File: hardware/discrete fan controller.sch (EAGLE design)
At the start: 13 parts, among them Q1 BCX56, U1 TL431

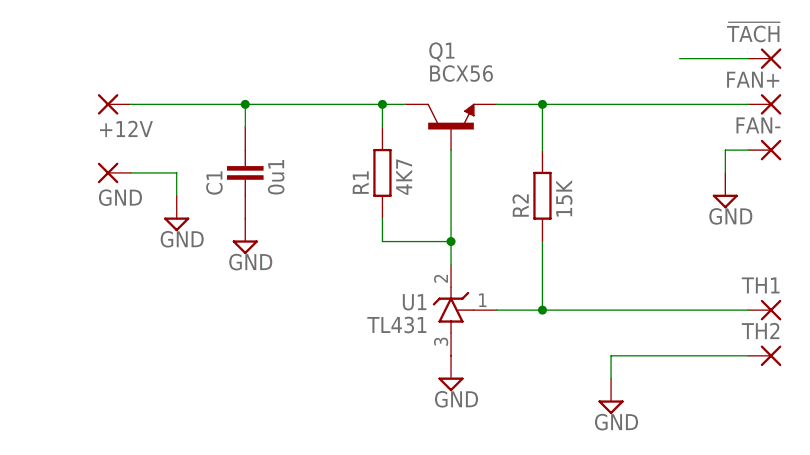
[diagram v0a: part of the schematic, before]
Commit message: TL431 Minimum current
4K7 changed to 1K.
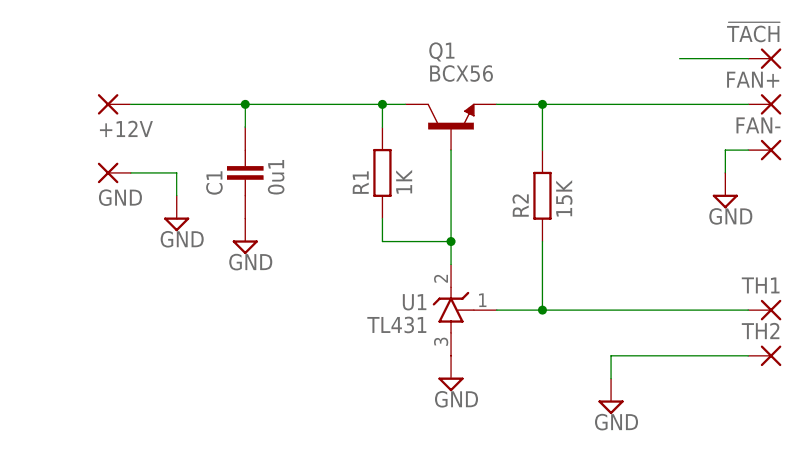
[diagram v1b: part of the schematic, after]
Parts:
- R1: value 4K7 -> 1K
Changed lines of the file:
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@@
 <part name="Q1" library="ipc-7351-transistor" deviceset="NPN_" device="SOT89" technology="SOT89" value="BCX56"/>
 <part name="U1" library="Misc Analog" deviceset="TL_431" device="DBZ" value="TL431"/>
-<part name="R1" library="ipc-7351-resistor" deviceset="RESISTOR_" device="0603" value="4K7"/>
+<part name="R1" library="ipc-7351-resistor" deviceset="RESISTOR_" device="0603" value="1K"/>
 <part name="R2" library="ipc-7351-resistor" deviceset="RESISTOR_" device="0603" value="15K"/>
 <part name="SUPPLY1" library="supply2" deviceset="GND" device=""/>
